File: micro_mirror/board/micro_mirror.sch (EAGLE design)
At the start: 162 parts, among them IC1 74LV7014, IC2 74LV02, IC3 74LV08, IC4 LM324D, IC5 LM324D, J1 POWER_JACKPTH_LOCK

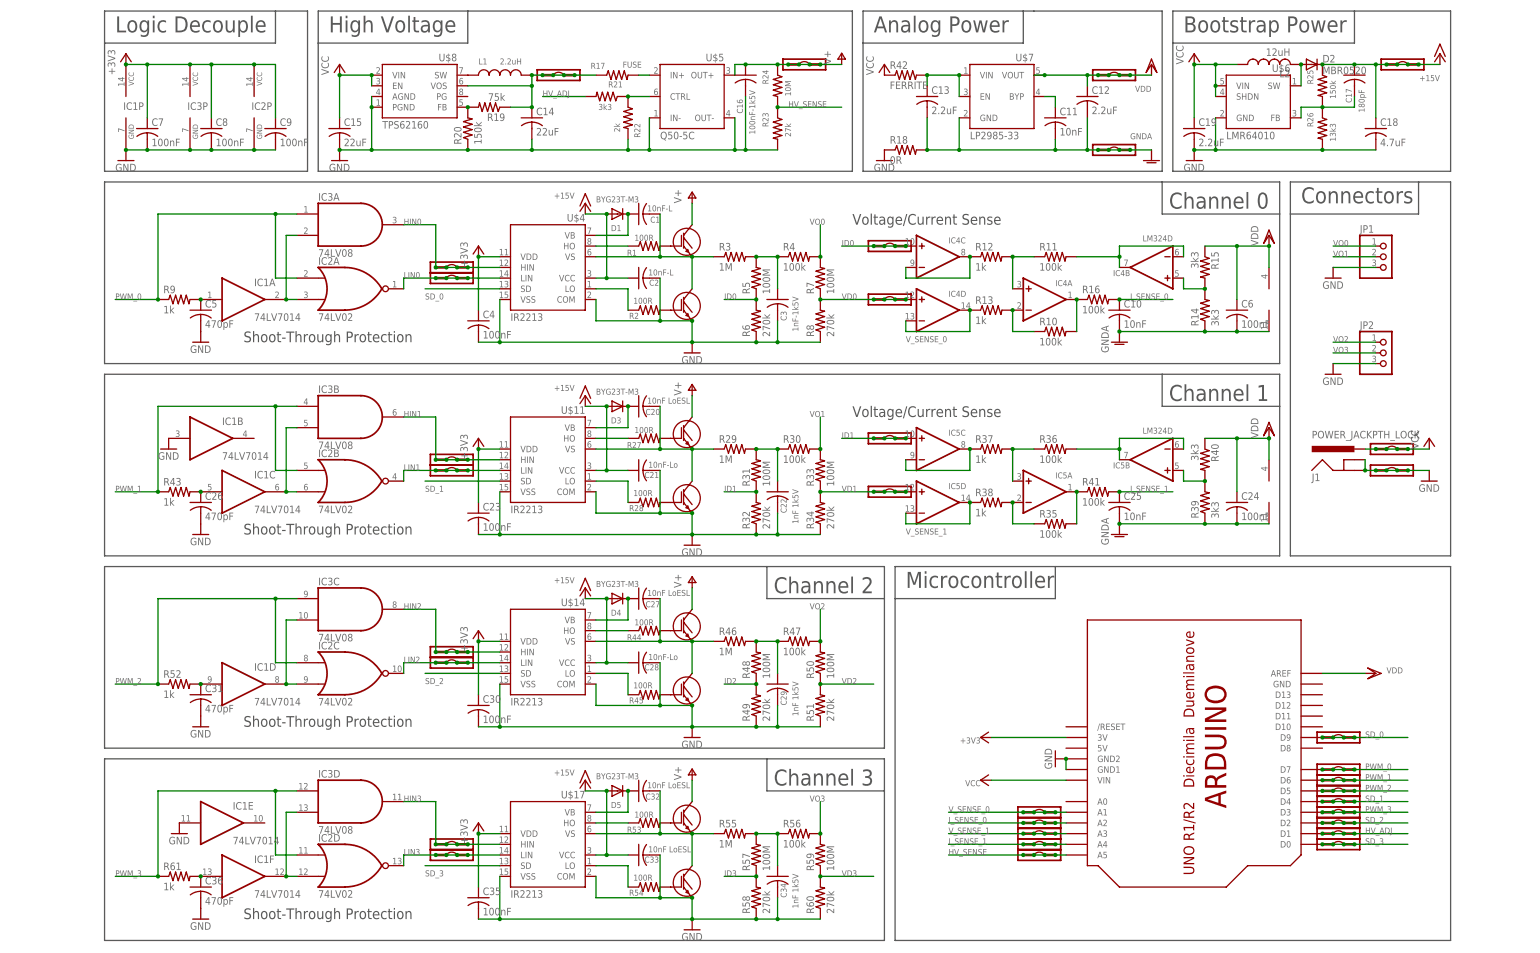
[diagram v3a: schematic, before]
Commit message: Tiled micro mirror board. Added author info etc. Used extra buffers in full channels for additional drive isolation. Added border.
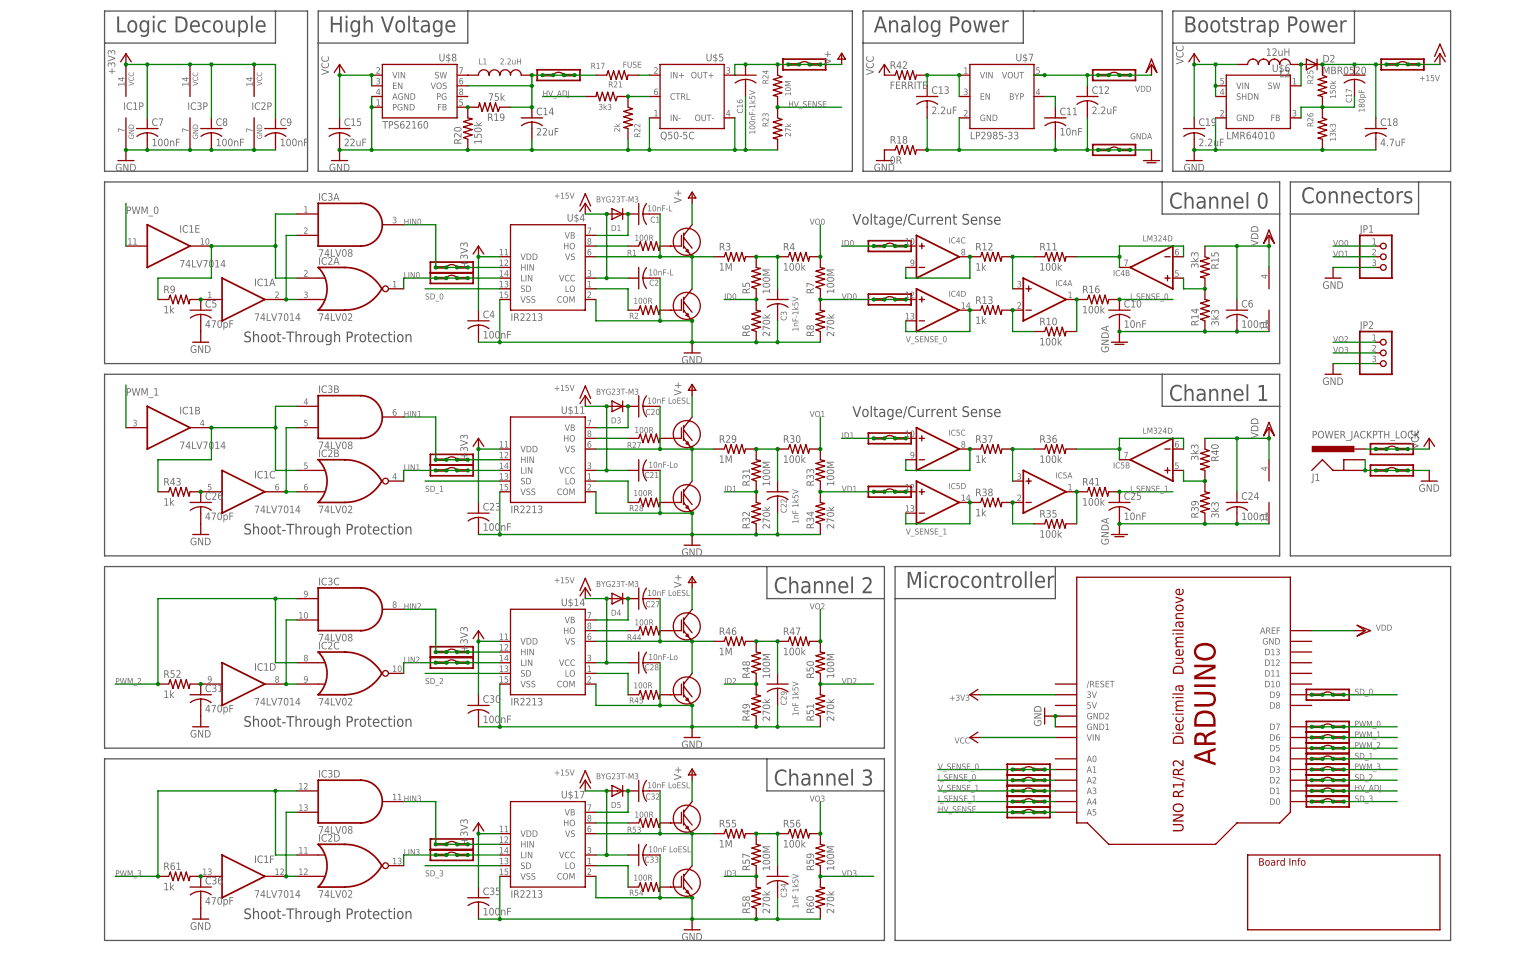
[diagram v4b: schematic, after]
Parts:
- added U$18: INFO, modular_robotics:INFO
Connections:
- new net N$58: IC1B.O, IC2B.I0, IC3B.I0, R43.1
- new net N$59: IC1E.O, IC2A.I0, IC3A.I0, R9.1
- net GND: no longer IC1B.I, IC1E.I
- net PWM_0: now also IC1E.I; no longer IC2A.I0, IC3A.I0, R9.1
- net PWM_1: now also IC1B.I; no longer IC2B.I0, IC3B.I0, R43.1
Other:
- moved on the sheet: IC1B, IC1E
